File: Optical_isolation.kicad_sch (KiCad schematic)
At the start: 76 parts, among them U601 ISO1541, U602 ISO6741

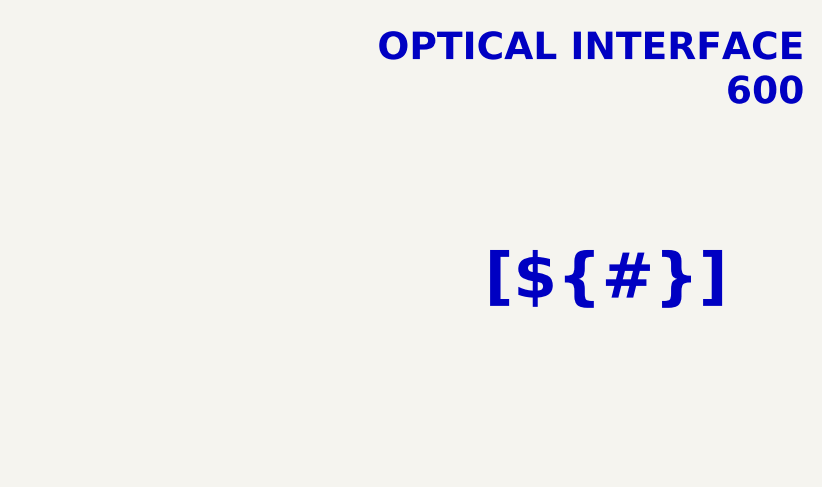
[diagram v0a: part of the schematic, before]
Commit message: Reworked sheet titles
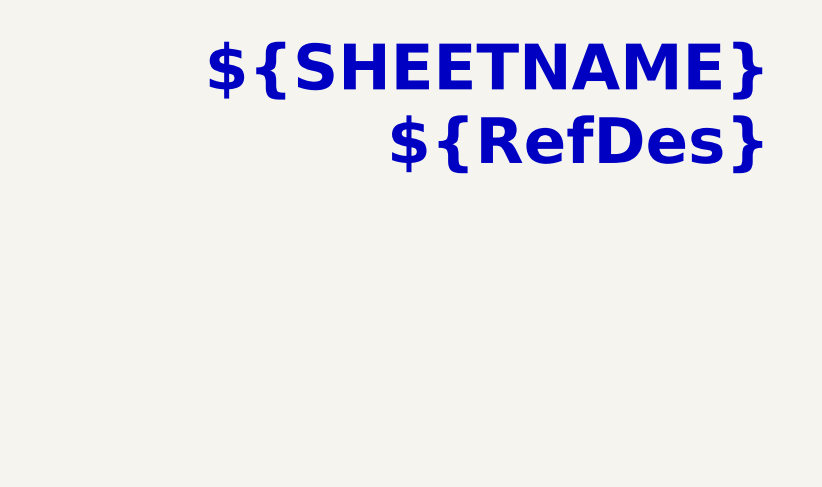
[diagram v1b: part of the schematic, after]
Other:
- note removed: "OPTICAL INTERFACE 600"
- title: (none) -> ${SHEETNAME}
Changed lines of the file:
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@@
 	(paper "A4")
 	(title_block
+		(title "${SHEETNAME}")
 		(date "2025-01-12")
 	)
@@
 		)
 	)
-	(text "OPTICAL INTERFACE\n600"
+	(text_box "${SHEETNAME}\n${RefDes}"
 		(exclude_from_sim no)
-		(at 283.21 19.05 0)
-		(effects
-			(font
-				(size 3.048 3.048)
-				(thickness 0.4064)
-				(bold yes)
-				(color 0 0 255 1)
-			)
-			(justify right)
-		)
-	)
-	(text_box "[${#}] ${TITLE}"
-		(exclude_from_sim no)
-		(at 179.07 35.56 0)
-		(size 101.6 12.7)
-		(margins 5.9999 5.9999 5.9999 5.9999)
+		(at 208.28 15.24 0)
+		(size 73.66 15.24)
+		(margins 2.54 1.27 2.54 1.27)
 		(stroke
 			(width -0.0001)

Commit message: Added PCB
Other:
- moved on the sheet: R619

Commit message: updating BOM info
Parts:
- C601, C602, C603, C604: Manufacturer (none) -> CCTC; Manufacturer Part Number (none) -> TCC0603X7R104K500CT
- R601, R602, R603, R604, R605, R606, R607, R608, R609, R610, R611, R612, R613, R614, R615, R616, R617, R618, R619: Manufacturer (none) -> Generic
- U601: Manufacturer (none) -> Texas Instruments; Manufacturer Part Number (none) -> ISO1541DR
- U602: Manufacturer (none) -> Texas Instruments; Manufacturer Part Number (none) -> ISO6741DWR

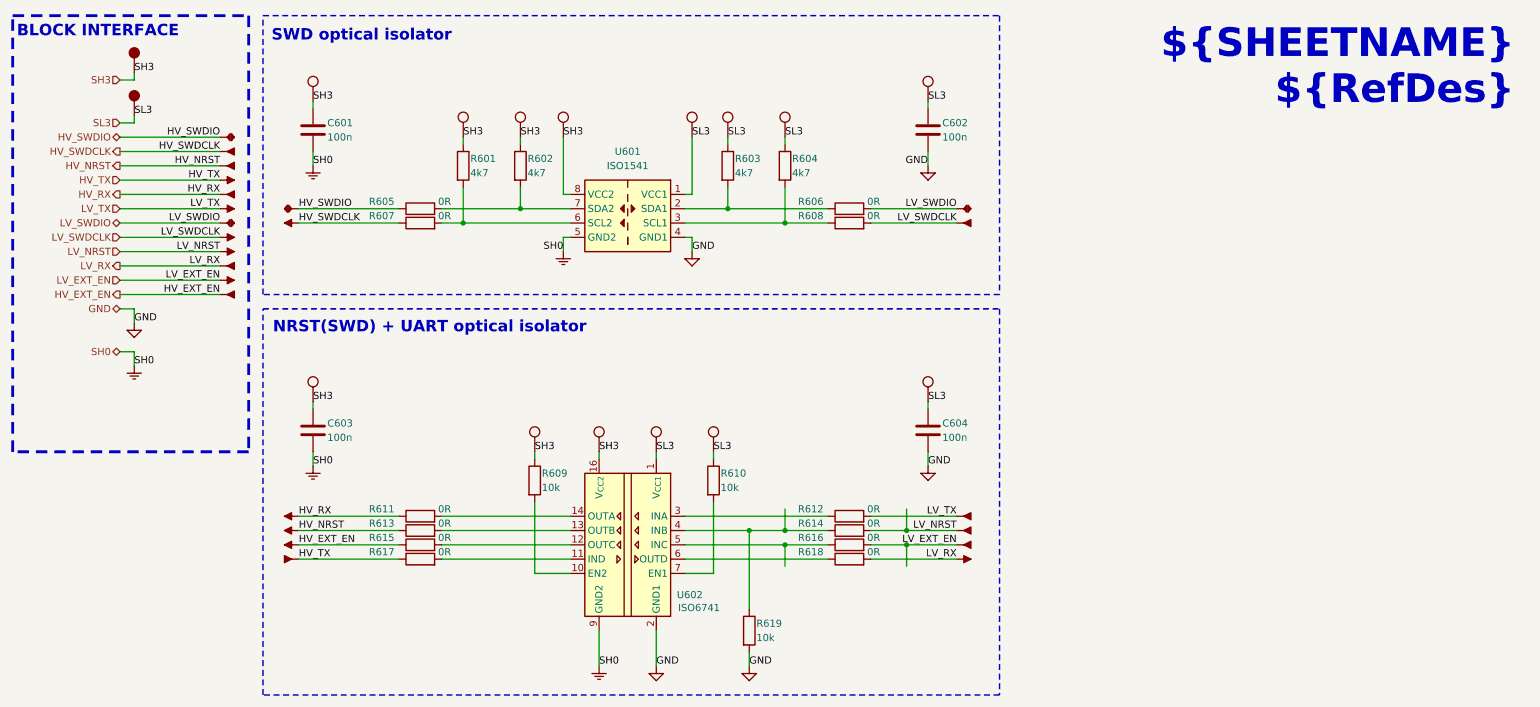
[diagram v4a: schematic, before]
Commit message: Reannotated, silk done, missing some 3D models
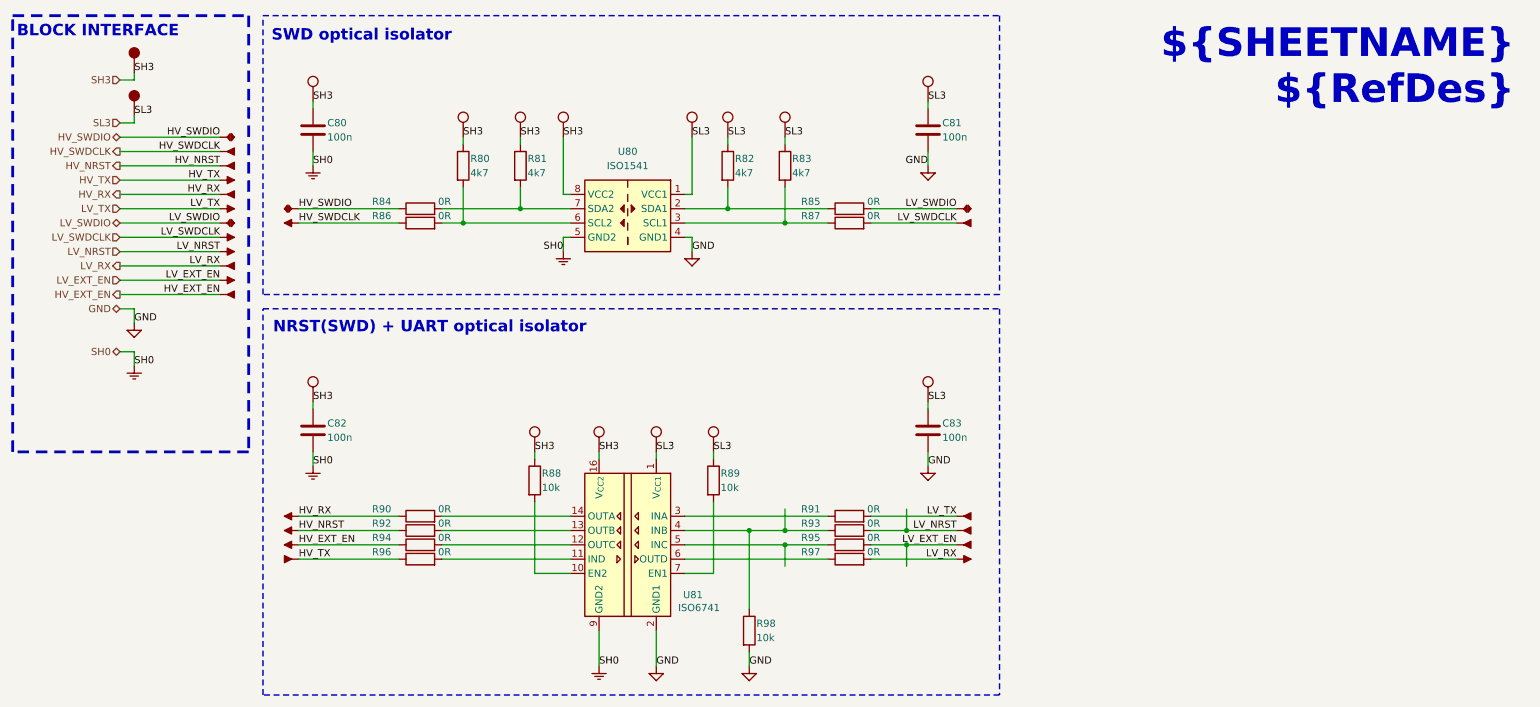
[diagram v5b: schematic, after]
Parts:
- renumbered C601 to C80, C602 to C81, C603 to C82, C604 to C83, P797 to P183, P841 to P184, P645 to P185, P798 to P186, P649 to P187, P840 to P188, P839 to P189, P838 to P190, P837 to P191, P836 to P192, P835 to P193, P686 to P194, P687 to P195, P832 to P196, P689 to P197, P690 to P198, P691 to P199, P692 to P200, P834 to P201, P694 to P202, P833 to P203, P696 to P204, P697 to P205, P730 to P206, P731 to P207, P704 to P208, P705 to P209, P695 to P210, P700 to P211, P703 to P212, P709 to P213, P710 to P214, P711 to P215, P712 to P216, P713 to P217, P714 to P218, P715 to P219, P716 to P220, P717 to P221, P718 to P222, P719 to P223, P720 to P224, P721 to P225, P722 to P226, P723 to P227, P724 to P228, P725 to P229, P726 to P230, P727 to P231, P728 to P232, P729 to P233, R601 to R80, R602 to R81, R603 to R82, R604 to R83, R605 to R84, R606 to R85, R607 to R86, R608 to R87, R609 to R88, R610 to R89, R611 to R90, R612 to R91, R613 to R92, R614 to R93, R615 to R94, R616 to R95, R617 to R96, R618 to R97, R619 to R98, U601 to U80, U602 to U81

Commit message: Changed to checked, updated fab pdf yaml
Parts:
- C80, C81, C82, C83: MAN (none) -> Generic; Manufacturer CCTC -> Generic; Manufacturer Part Number TCC0603X7R104K500CT -> (none)
- R80, R81, R82, R83, R84, R85, R86, R87, R88, R89, R90, R91, R92, R93, R94, R95, R96, R97, R98: MAN (none) -> Generic
- U80: MAN (none) -> Texas Instruments; MPN (none) -> ISO1541DR
- U81: MAN (none) -> Texas Instruments; MPN (none) -> ISO6741DWR
